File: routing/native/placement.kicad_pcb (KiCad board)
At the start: 4 copper layers, 46 x 46 mm, 71 parts, among them J1 J1, J2 J2, J3 J3, J4 J4, J5 J5, M1 M1, Q1 Q1, Q2 Q2, SW1 SW1, SW2 SW2, U1 NRF52810-QFAA-R, U2 BMA456, U3 HUSB238_002DD, U4 PCF8563TS/5,118, U5 BQ25180YBGR, U6 TPS63802DLAR, Y1 Y1, Y2 Y2, Y3 Y3

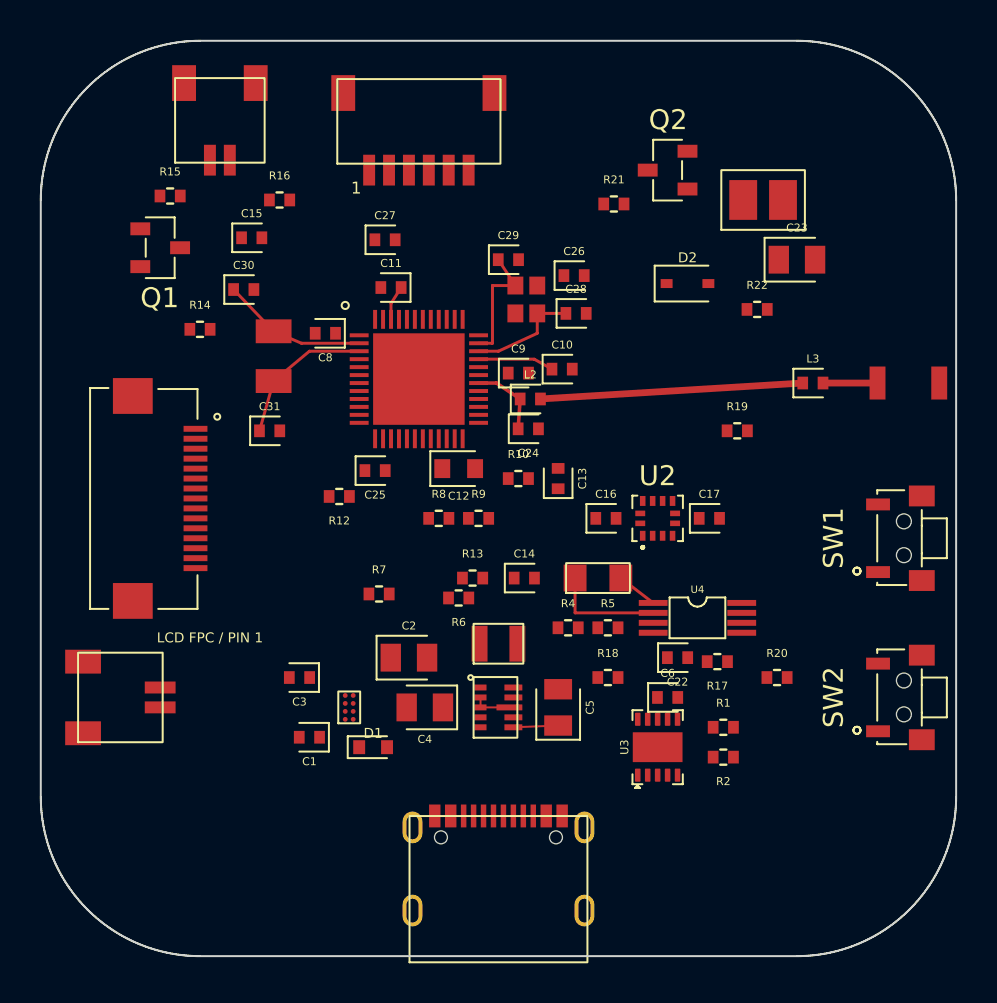
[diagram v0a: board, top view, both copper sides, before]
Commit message: Move charging port opposite centred buttons and reroute the assembly
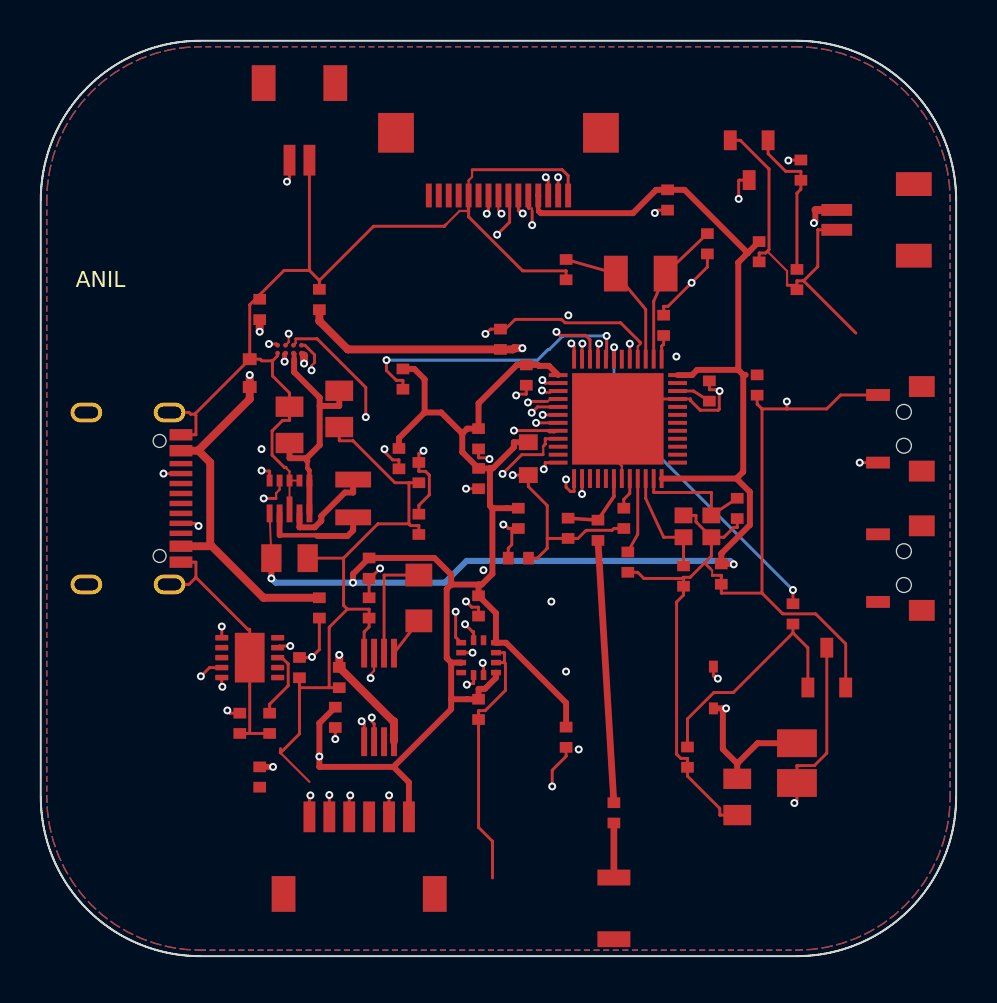
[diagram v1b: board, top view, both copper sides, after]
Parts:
- ANT1: footprint tscircuit:RFANT3216120A5T -> Smartwatch:ANT1_exact
- C1: footprint tscircuit:CL05A105KA5NQNC -> Smartwatch:C1_exact
- C10: footprint tscircuit:CC0402KRX7R7BB104 -> Smartwatch:C10_exact
- C11: footprint tscircuit:CL05A105KA5NQNC -> Smartwatch:C11_exact
- C12: footprint tscircuit:CL10A475KO8NNNC -> Smartwatch:C12_exact
- C13: footprint tscircuit:CC0402KRX7R7BB104 -> Smartwatch:C13_exact
- C14: footprint tscircuit:CC0402KRX7R7BB104 -> Smartwatch:C14_exact
- C15: footprint tscircuit:CC0402KRX7R7BB104 -> Smartwatch:C15_exact
- C16: footprint tscircuit:CC0402KRX7R7BB104 -> Smartwatch:C16_exact
- C17: footprint tscircuit:CC0402KRX7R7BB104 -> Smartwatch:C17_exact
- C2: footprint tscircuit:CL21A106KAYNNNE -> Smartwatch:C2_exact
- C22: footprint tscircuit:CC0402KRX7R7BB104 -> Smartwatch:C22_exact
- C23: footprint tscircuit:CL21A226MAQNNNE -> Smartwatch:C23_exact
- C24: footprint tscircuit:GJM1555C1HR80WB01D -> Smartwatch:C24_exact
- C25: footprint tscircuit:CC0402KRX7R7BB104 -> Smartwatch:C25_exact
- C26: footprint tscircuit:CC0402KRX7R7BB104 -> Smartwatch:C26_exact
- C27: footprint tscircuit:CC0402KRX7R7BB104 -> Smartwatch:C27_exact
- C28: footprint tscircuit:0402CG120J500NT -> Smartwatch:C28_exact
- C29: footprint tscircuit:0402CG120J500NT -> Smartwatch:C29_exact
- C3: footprint tscircuit:CL05A105KA5NQNC -> Smartwatch:C3_exact
- C30: footprint tscircuit:0402CG120J500NT -> Smartwatch:C30_exact
- C31: footprint tscircuit:0402CG120J500NT -> Smartwatch:C31_exact
- C4: footprint tscircuit:CL21A106KAYNNNE -> Smartwatch:C4_exact
- C5: footprint tscircuit:CL21A226MAQNNNE -> Smartwatch:C5_exact
- C6: footprint tscircuit:CL05A105KA5NQNC -> Smartwatch:C6_exact
- C8: footprint tscircuit:CC0402KRX7R7BB104 -> Smartwatch:C8_exact
- C9: footprint tscircuit:0402CG101J500NT -> Smartwatch:C9_exact
- D1: footprint tscircuit:LESD5Z5_0CT1G -> Smartwatch:D1_exact
- D2: footprint tscircuit:1N5819WS -> Smartwatch:D2_exact
- J1: footprint tscircuit:TYPE-C-31-M-12 -> Smartwatch:J1_exact
- J2: footprint tscircuit:SM02B-SRSS-TB_LF_SN -> Smartwatch:J2_exact
- J3: footprint tscircuit:SM06B-SRSS-TB_LF_SN -> Smartwatch:J3_exact
- J4: footprint tscircuit:AFC24-S15FIA-00 -> Smartwatch:J4_exact
- J5: footprint tscircuit:SM02B-SRSS-TB_LF_SN -> Smartwatch:J5_exact
- L1: footprint tscircuit:DFE252012P-R47M_P2 -> Smartwatch:L1_exact
- L2: footprint tscircuit:LQG15HS3N9S02D -> Smartwatch:L2_exact
- L3: footprint tscircuit:LQG15HS6N8J02D -> Smartwatch:L3_exact
- M1: footprint tscircuit:LCM1234A3523F -> Smartwatch:M1_exact
- Q1: footprint tscircuit:2N7002 -> Smartwatch:Q1_exact
- Q2: footprint tscircuit:AO3400A -> Smartwatch:Q2_exact
- R1: footprint tscircuit:0402WGF0000TCE -> Smartwatch:R1_exact
- R10: footprint tscircuit:0402WGF1002TCE -> Smartwatch:R10_exact
- R12: footprint tscircuit:0402WGF1004TCE -> Smartwatch:R12_exact
- R13: footprint tscircuit:0402WGF3303TCE -> Smartwatch:R13_exact
- R14: footprint tscircuit:0402WGF220JTCE -> Smartwatch:R14_exact
- R15: footprint tscircuit:0402WGF1000TCE -> Smartwatch:R15_exact
- R16: footprint tscircuit:0402WGF1003TCE -> Smartwatch:R16_exact
- R17: footprint tscircuit:0402WGF1002TCE -> Smartwatch:R17_exact
- R18: footprint tscircuit:0402WGF100JTCE -> Smartwatch:R18_exact
- R19: footprint tscircuit:0402WGF1003TCE -> Smartwatch:R19_exact
- R2: footprint tscircuit:0402WGF0000TCE -> Smartwatch:R2_exact
- R20: footprint tscircuit:0402WGF1003TCE -> Smartwatch:R20_exact
- R21: footprint tscircuit:0402WGF1000TCE -> Smartwatch:R21_exact
- R22: footprint tscircuit:0402WGF1003TCE -> Smartwatch:R22_exact
- R4: footprint tscircuit:RC0402FR-07510KL -> Smartwatch:R4_exact
- R5: footprint tscircuit:0402WGF1003TCE -> Smartwatch:R5_exact
- R6: footprint tscircuit:0402WGF1003TCE -> Smartwatch:R6_exact
- R7: footprint tscircuit:0402WGF1002TCE -> Smartwatch:R7_exact
- R8: footprint tscircuit:0402WGF4701TCE -> Smartwatch:R8_exact
- R9: footprint tscircuit:0402WGF4701TCE -> Smartwatch:R9_exact
- SW1: footprint tscircuit:TS-1806SA-2x4x3_5DY-180X -> Smartwatch:SW1_exact
- SW2: footprint tscircuit:TS-1806SA-2x4x3_5DY-180X -> Smartwatch:SW2_exact
- U1: footprint tscircuit:NRF52810-QFAA-R -> Smartwatch:U1_exact
- U2: footprint tscircuit:BMA456 -> Smartwatch:U2_exact
- U3: footprint tscircuit:HUSB238_002DD -> Smartwatch:U3_exact
- U4: footprint tscircuit:PCF8563TS_5_118 -> Smartwatch:U4_exact
- U5: footprint tscircuit:BQ25180YBGR -> Smartwatch:U5_exact
- U6: footprint tscircuit:TPS63802DLAR -> Smartwatch:U6_exact
- Y1: footprint tscircuit:FC-135_32_7680KA-AG3 -> Smartwatch:Y1_exact
- Y2: footprint tscircuit:X201632MKB4SI -> Smartwatch:Y2_exact
- Y3: footprint tscircuit:ABS07-32_768KHZ-9-T -> Smartwatch:Y3_exact
- moved J3 36.6 mm to (93.0, 118.0), turned to 180 degrees
- moved J2 33.4 mm to (119.0, 86.0), turned to -90 degrees
- moved R15 31.7 mm to (115.2, 83.5), turned to -90 degrees
- moved J5 30.4 mm to (90.0, 81.0), turned to 0 degrees
- moved ANT1 30.3 mm to (105.8, 120.6), turned to -90 degrees
- moved Q1 29.9 mm to (112.6, 83.0), turned to 90 degrees
- moved M1 28.4 mm to (115.0, 113.3), turned to -90 degrees
- moved C23 27.2 mm to (112.0, 115.0), turned to -90 degrees
- moved R20 26.5 mm to (88.0, 114.0), turned to -90 degrees
- moved R16 26.3 mm to (115.0, 89.0), turned to -90 degrees
- moved Q2 26.2 mm to (116.5, 108.5), turned to -90 degrees
- moved J1 26.1 mm to (81.6, 100.0), turned to -90 degrees
- moved C15 25.5 mm to (113.1, 87.6), turned to -90 degrees
- moved R14 24.4 mm to (108.5, 85.0), turned to -90 degrees
- moved R2 24.4 mm to (87.0, 111.3), turned to -90 degrees
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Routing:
- net GND: track 1.95 -> 284.2 mm, vias 0 -> 7
- net V3V0: track 2.25 -> 153.4 mm, vias 0 -> 6
- net BAT: track 0.00 -> 64.5 mm, vias 0 -> 4
- net I2C_SDA: track 0.00 -> 50.4 mm, vias 0 -> 5
- net BUTTON1: track 0.00 -> 41.1 mm, vias 0 -> 3
- net I2C_SCL: track 0.00 -> 38.1 mm, vias 0 -> 5
- net SWCLK: track 0.00 -> 25.7 mm, vias 0 -> 3
- net SWDIO: track 0.00 -> 25.6 mm, vias 0 -> 3
- net NRST: track 0.00 -> 25.4 mm, vias 0 -> 3
- net USB5V: track 0.00 -> 25.3 mm, vias 0 -> 3
- net DEBUG_GPIO: track 0.00 -> 25.2 mm, vias 0 -> 2
- net RTC_INT: track 0.00 -> 23.6 mm, vias 0 -> 3
- net LCD_BL: track 0.00 -> 21.2 mm, vias 0 -> 3
- net BAT_ADC: track 0.00 -> 20.6 mm, vias 0 -> 2
- net CHG_INT: track 0.00 -> 20.4 mm, vias 0 -> 3
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- added copper zone on B.Cu, net GND
- added copper zone on F.Cu, net GND
- added copper zone on In1.Cu, net GND
- added copper zone on In2.Cu, net GND
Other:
- board text added: "ANIL"
- board text removed: "LCD FPC / PIN 1"
